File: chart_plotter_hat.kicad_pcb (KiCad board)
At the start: 4 copper layers, 65 x 56 mm, 52 parts, among them J1 Conn_02x03_Odd_Even, J2 Conn_01x04, J3 40HAT, J4 Conn_01x04, J5 Conn_01x04, J6 Conn_01x02, J7 Conn_01x04, J8 Conn_02x03_Odd_Even, J9 Conn_01x04, Q1 DMG2305UX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

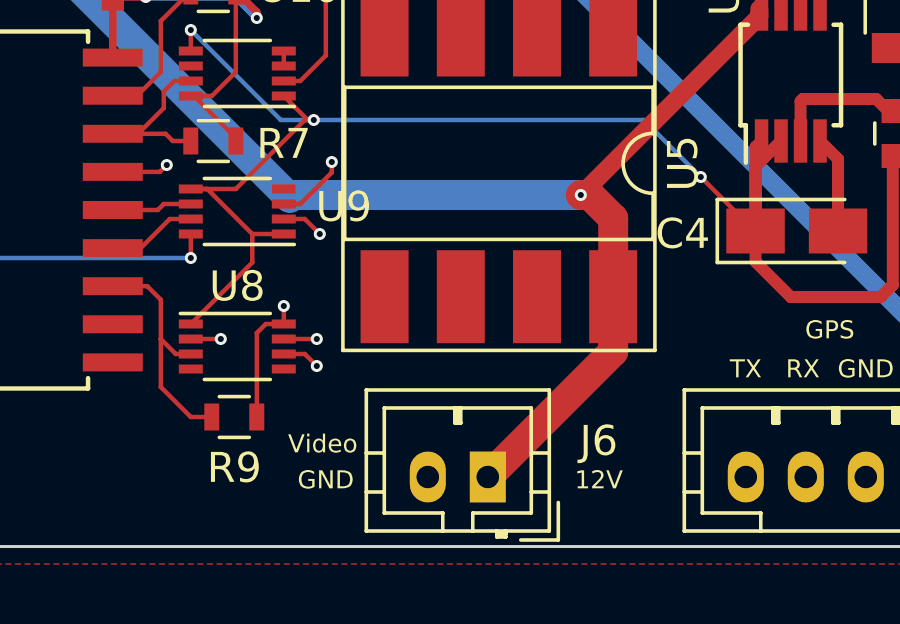
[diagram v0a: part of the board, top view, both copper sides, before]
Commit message: Fixed relay wiring
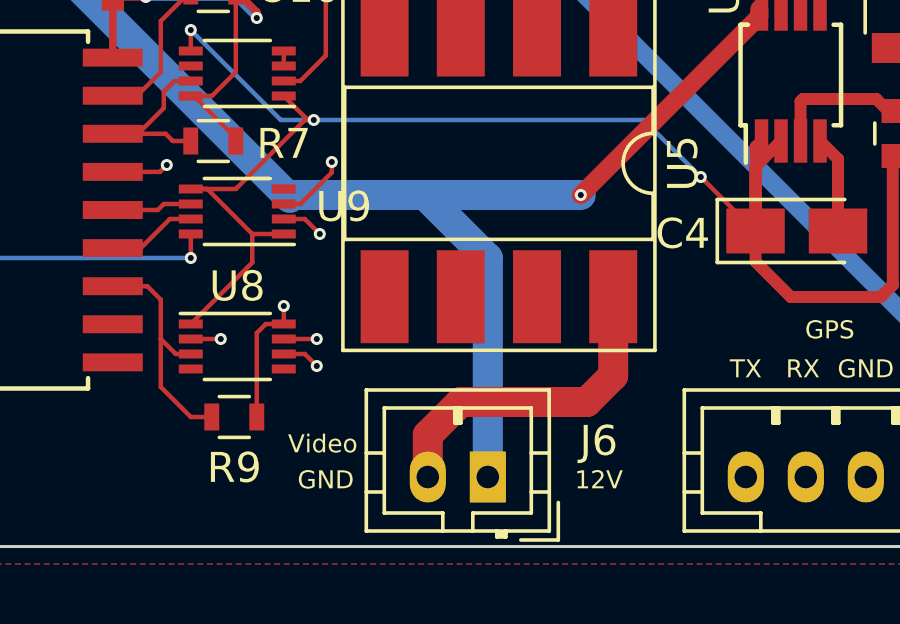
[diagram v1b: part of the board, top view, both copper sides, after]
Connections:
- J6 pad 2: GND -> Net-(J6-Pad2)
- U5 pad 8: +12V -> Net-(J6-Pad2)
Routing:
- net Net-(J6-Pad2): track 0.00 -> 11.0 mm
- net +12V: track 92.2 -> 90.7 mm

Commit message: Updated from rev B
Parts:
- added C12: .1uF, Capacitors_SMD:C_0603, F.Cu at (100.3, 96.0)
- added C13: .1uF, Capacitors_SMD:C_0603, F.Cu at (166.4, 97.2)
- added C14: .1uF, Capacitors_SMD:C_0603, F.Cu at (173.0, 90.8)
- added C15: .1uF, Capacitors_SMD:C_0603, F.Cu at (88.7, 101.3)
- added C16: 18pF, Capacitors_SMD:C_0603, F.Cu at (176.8, 88.4)
- added C17: 18pF, Capacitors_SMD:C_0603, F.Cu at (173.0, 93.1)
- added D3: PMEG3020EH, Diodes_SMD:D_SOD-123, F.Cu at (82.6, 95.5)
- added JP1: SolderJumper_2_Open, CustomComponents:SolderJumper-2_P1.3mm_Open_RoundedPad1.0x1.5mm, F.Cu at (134.1, 88.5)
- added L1: 10uH, Capacitors_SMD:C_0603, F.Cu at (130.7, 90.4)
- added R11: 10K, Resistors_SMD:R_0603, F.Cu at (176.7, 90.8)
- added R12: 10K, Resistors_SMD:R_0603, F.Cu at (180.5, 87.7)
- added R13: 10K, Resistors_SMD:R_0603, F.Cu at (174.0, 95.5)
- C10, C11: value 18pF -> .1uF
- J1: value Conn_02x03_Odd_Even -> JST PH; footprint CustomComponents:BOX-HEADER6 -> Connectors_JST:JST_PH_B6B-PH-K_06x2.00mm_Straight
- J2, J4, J5, J7: value Conn_01x04 -> JST PH
- J6: value Conn_01x02 -> JST PH
- J9: value Conn_01x04 -> JST PH; footprint Connectors_JST:JST_PH_B4B-PH-K_04x2.00mm_Straight -> Connectors_JST:JST_PH_B3B-PH-K_03x2.00mm_Straight
- R2, R4: value 680 -> 1.6K
- R3: value 330 -> 750
- R7: value 10K -> 39K
- R9: value 10K -> 12K
- U6: value MCP2551-I-SN -> MCP2515-xSO; footprint Housings_SOIC:SOIC-8_3.9x4.9mm_Pitch1.27mm -> Housings_SOIC:SOIC-18W_7.5x11.6mm_Pitch1.27mm
- U7: value MCP2515-xSO -> MCP2551-I-SN; footprint Housings_SOIC:SOIC-18W_7.5x11.6mm_Pitch1.27mm -> Housings_SOIC:SOIC-8_3.9x4.9mm_Pitch1.27mm
- Y1: value 16MHz -> 16 MHz
- moved C11 90.5 mm to (177.4, 85.3)
- moved C10 88.3 mm to (173.0, 88.4)
- moved Y1 85.9 mm to (166.6, 83.9)
- moved C9 76.2 mm to (164.4, 94.8), turned to 0 degrees
- moved U9 74.8 mm to (178.2, 82.3), turned to 0 degrees
- moved R5 74.6 mm to (180.5, 90.2)
- moved C8 67.3 mm to (170.3, 97.2), turned to 0 degrees
- moved U8 52.8 mm to (157.9, 95.7)
- moved U10 45.5 mm to (152.3, 95.7), turned to 0 degrees
- moved J9 38.7 mm to (117.6, 114.2), turned to 180 degrees
- moved R9 27.8 mm to (131.2, 98.8)
- moved R7 26.0 mm to (131.2, 95.6), turned to 180 degrees
- moved R3 21.4 mm to (74.7, 96.8)
- moved D2 20.9 mm to (74.3, 94.1)
- moved D1 20.7 mm to (74.3, 89.7)
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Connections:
- net SS renamed CS
- C10 pad 1: Net-(C10-Pad1) -> GND
- C10 pad 2: GND -> +3V3
- C11 pad 1: Net-(C11-Pad1) -> GND
- C11 pad 2: GND -> +5V
- C5 pad 1: +3V3 -> Net-(C5-Pad1)
- C8 pad 1: +5V -> GND
- C8 pad 2: GND -> +3V3
- C9 pad 1: +5V -> GND
- C9 pad 2: GND -> +5V
- D2 pad 2: SHUTDOWN -> Net-(D2-Pad2)
- J2 pad 1: +12V -> /12VBAT
- J3 pad 11: CAN_INT -> (no net)
- J3 pad 12: XCLR -> CAN_CS
- J3 pad 13: (no net) -> BUTTON
- J3 pad 18: (no net) -> XCLR
- J3 pad 26: CSS -> (no net)
- J3 pad 35: (no net) -> MISO-2
- J3 pad 36: (no net) -> CAN_RST
- J3 pad 38: (no net) -> MOSI-2
- J3 pad 40: (no net) -> SCK-2
- J6 pad 1: +12V -> Net-(J6-Pad1)
- J6 pad 2: Net-(J6-Pad2) -> GND
- J9 pad 1: +12V -> /12VBAT
- J9 pad 2: Net-(J9-Pad2) -> +5V
- J9 pad 3: Net-(J9-Pad3) -> GND
- R2 pad 2: +5V -> GND
- R5 pad 1: Net-(R5-Pad1) -> CAN_INT
- R5 pad 2: +5V -> +3V3
- R7 pad 1: CAN-SS -> /12VBAT
- R7 pad 2: +5V -> Net-(JP1-Pad2)
- R9 pad 1: INT -> GND
- R9 pad 2: +5V -> Net-(JP1-Pad2)
- U1 pad 1: MCU_RUNNING -> (no net)
- U1 pad 12: (no net) -> Net-(D2-Pad2)
- U1 pad 13: (no net) -> MCU_RUNNING
- U1 pad 18: +3V3 -> Net-(C5-Pad1)
- U10 pad 2: CSS -> CAN_CS
- U10 pad 3: GND -> CAN_RST
- U10 pad 6: GND -> CRST
- U10 pad 7: CAN-SS -> CCS
- U5 pad 2: Net-(R2-Pad1) -> +5V
- U5 pad 3: GND -> Net-(R2-Pad1)
- U5 pad 5: GND -> Net-(J6-Pad1)
- U5 pad 8: Net-(J6-Pad2) -> +12V
- U6 pad 2: GND -> Net-(U6-Pad2)
- U6 pad 3: +5V -> (no net)
- U6 pad 4: Net-(U6-Pad4) -> (no net)
- U6 pad 6: Net-(J9-Pad2) -> (no net)
- U6 pad 7: Net-(J9-Pad3) -> Net-(C16-Pad1)
- U6 pad 8: GND -> Net-(C17-Pad1)
- U7 pad 2: Net-(U6-Pad4) -> GND
- U7 pad 3: (no net) -> +5V
- U7 pad 4: (no net) -> Net-(U6-Pad2)
- U7 pad 7: Net-(C10-Pad1) -> (no net)
- U7 pad 8: Net-(C11-Pad1) -> GND
- U8 pad 2: CAN-MISO -> CAN_INT
- U8 pad 3: INT -> MISO-2
- U8 pad 6: CAN_INT -> CAN_SO
- U8 pad 7: MISO -> INT
- U9 pad 2: SCK -> MOSI-2
- U9 pad 3: MOSI -> SCK-2
- U9 pad 6: CAN-MOSI -> CAN_SCK
- U9 pad 7: CAN-SCK -> CAN_SI
- Y1 pad 1: Net-(C10-Pad1) -> Net-(C16-Pad1)
- Y1 pad 2: Net-(C11-Pad1) -> Net-(C17-Pad1)
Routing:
- net +5V: track 134.3 -> 8.59 mm, vias 8 -> 0
- net +12V: track 90.7 -> 16.6 mm, vias 1 -> 0
- net SerialRX: track 66.1 -> 0.00 mm
- net SerialTX: track 65.4 -> 0.00 mm, vias 1 -> 0
- net CAN_INT: track 63.1 -> 0.00 mm, vias 2 -> 0
- net +3V3: track 172.3 -> 116.4 mm, vias 9 -> 4
- net CSS: track 42.9 -> 0.00 mm, vias 2 -> 0
- net SHUTDOWN: track 59.3 -> 34.8 mm, vias 4 -> 1
- net SCK: track 77.0 -> 53.7 mm, vias 3 -> 1
- net MISO: track 78.6 -> 56.7 mm, vias 3 -> 2
- net BUTTON: track 43.0 -> 63.0 mm, vias 1 -> 2
- net MOSI: track 76.3 -> 57.4 mm, vias 2 -> 1
- net Net-(C10-Pad1): track 16.5 -> 0.00 mm
- net MCU_RUNNING: track 32.7 -> 47.7 mm, vias 1 -> 2
- net Net-(JP1-Pad2): track 0.00 -> 11.8 mm
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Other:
- board text added: "Barometer"
- board text added: "Rev C"
- board text added: "Sense"
- board text added: "Voltmeter"
- board text removed: "Hi"
- board text removed: "Lo"
- board text removed: "Pressure"
- board text removed: "Rev B"

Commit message: First pass at layout
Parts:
- removed C13, C14, C8, C9: .1uF, Capacitors_SMD:C_0603
- removed U10, U9: 74LVC2T45DC, Housings_SSOP:VSSOP-8_2.3x2mm_Pitch0.5mm
- added H5: LightPipeMount, project_footprints:SMFLPX.X-light-pipe-adapter-smd, F.Cu at (82.9, 103.8)
- added H6: LightPipeMount, project_footprints:SMFLPX.X-light-pipe-adapter-smd, F.Cu at (131.2, 106.7)
- added J10: JST PH, Connectors_JST:JST_PH_B2B-PH-K_02x2.00mm_Straight, F.Cu at (90.9, 114.1)
- added Q3: DMG2305UX, TO_SOT_Packages_SMD:SOT-23, F.Cu at (107.5, 88.2)
- added R14: 47K, Resistors_SMD:R_0603, F.Cu at (107.3, 84.5)
- U8: value 74LVC2T45DC -> ST2378E; footprint Housings_SSOP:VSSOP-8_2.3x2mm_Pitch0.5mm -> Housings_SSOP:TSSOP-20_4.4x6.5mm_Pitch0.65mm
- Y1: footprint Crystals:Crystal_HC49-U_Vertical -> Crystals:Crystal_SMD_SeikoEpson_TSX3225-4pin_3.2x2.5mm
- moved C16 82.9 mm to (97.8, 113.5)
- moved C17 74.2 mm to (101.7, 113.5), turned to 180 degrees
- moved Y1 72.0 mm to (99.7, 110.6)
- moved R3 66.8 mm to (140.4, 108.8)
- moved R5 62.2 mm to (120.0, 75.8), turned to 180 degrees
- moved R12 61.3 mm to (120.0, 77.8), turned to 180 degrees
- moved D2 58.3 mm to (131.2, 106.7), turned to 90 degrees
- moved C10 48.1 mm to (128.4, 70.2), turned to 180 degrees
- moved C11 47.1 mm to (132.8, 70.2)
- moved R13 44.4 mm to (136.1, 72.4), turned to 270 degrees
- moved R11 43.0 mm to (136.1, 76.5), turned to 270 degrees
- moved U8 34.0 mm to (130.6, 75.4)
- moved D1 16.5 mm to (82.9, 103.8)
- moved R4 9.74 mm to (82.8, 96.8)
- moved C12 8.76 mm to (91.5, 96.4), turned to 0 degrees
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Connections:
- C10 pad 2: +3V3 -> VEE
- C6 pad 1: +3V3 -> VEE
- J1 pad 1: +3V3 -> VEE
- J3 pad 37: (no net) -> CAN_INT
- R12 pad 2: +3V3 -> VEE
- R29 pad 1: +3V3 -> VEE
- R5 pad 2: +3V3 -> VEE
- R6 pad 1: +3V3 -> VEE
- R8 pad 1: +3V3 -> VEE
- U1 pad 11: (no net) -> VEE_ENABLE
- U2 pad 8: +3V3 -> VEE
- U7 pad 6: (no net) -> CAN_LO
- U7 pad 7: (no net) -> CAN_HI
- U8 pad 1: +3V3 -> VEE
- U8 pad 3: MISO-2 -> CAN_SO
- U8 pad 4: GND -> MOSI-2
- U8 pad 5: GND -> CAN_SCK
- U8 pad 6: CAN_SO -> CAN_CS
- U8 pad 7: INT -> CRST
- U8 pad 8: +5V -> (no net)
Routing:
- net +5V: track 8.59 -> 167.6 mm, vias 0 -> 5
- net /12VBAT: track 9.63 -> 92.6 mm
- net VEE: track 0.00 -> 81.3 mm, vias 0 -> 6
- net SerialRX: track 0.00 -> 73.4 mm
- net SerialTX: track 0.00 -> 70.8 mm, vias 0 -> 1
- net CCS: track 0.00 -> 53.9 mm, vias 0 -> 2
- net INT: track 0.00 -> 52.9 mm, vias 0 -> 3
- net CAN_SI: track 0.00 -> 50.9 mm, vias 0 -> 2
- net +12V: track 16.6 -> 61.8 mm, vias 0 -> 2
- net CRST: track 0.00 -> 41.5 mm, vias 0 -> 2
- net CAN_SO: track 0.00 -> 40.4 mm, vias 0 -> 2
- net CAN_CS: track 0.00 -> 38.8 mm, vias 0 -> 2
- net CAN_SCK: track 0.00 -> 38.1 mm, vias 0 -> 2
- net A7: track 15.7 -> 52.6 mm
- net A6: track 12.3 -> 45.5 mm, vias 1 -> 2
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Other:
- board text added: "CAN"
- board text added: "HI"
- board text added: "LO"

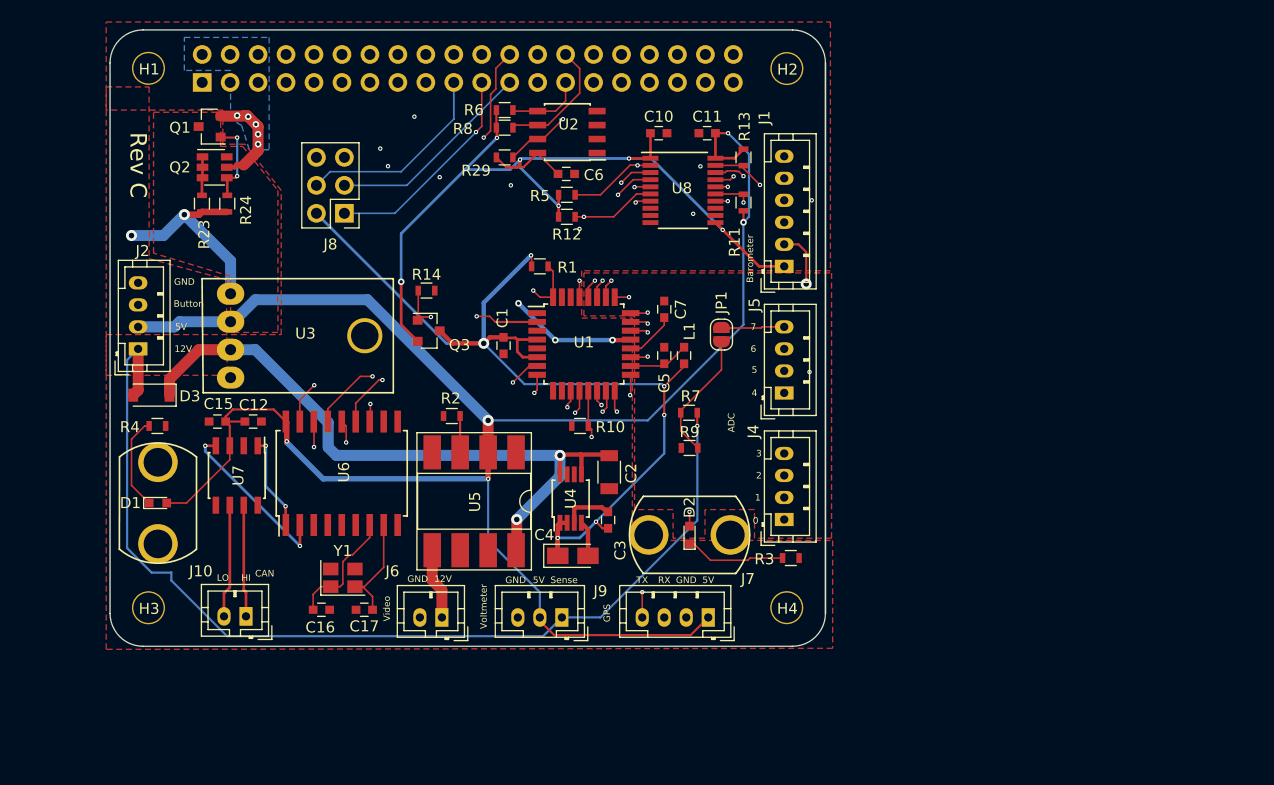
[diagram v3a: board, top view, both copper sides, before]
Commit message: Fixed 3.3aux switch and mounting hole sizes
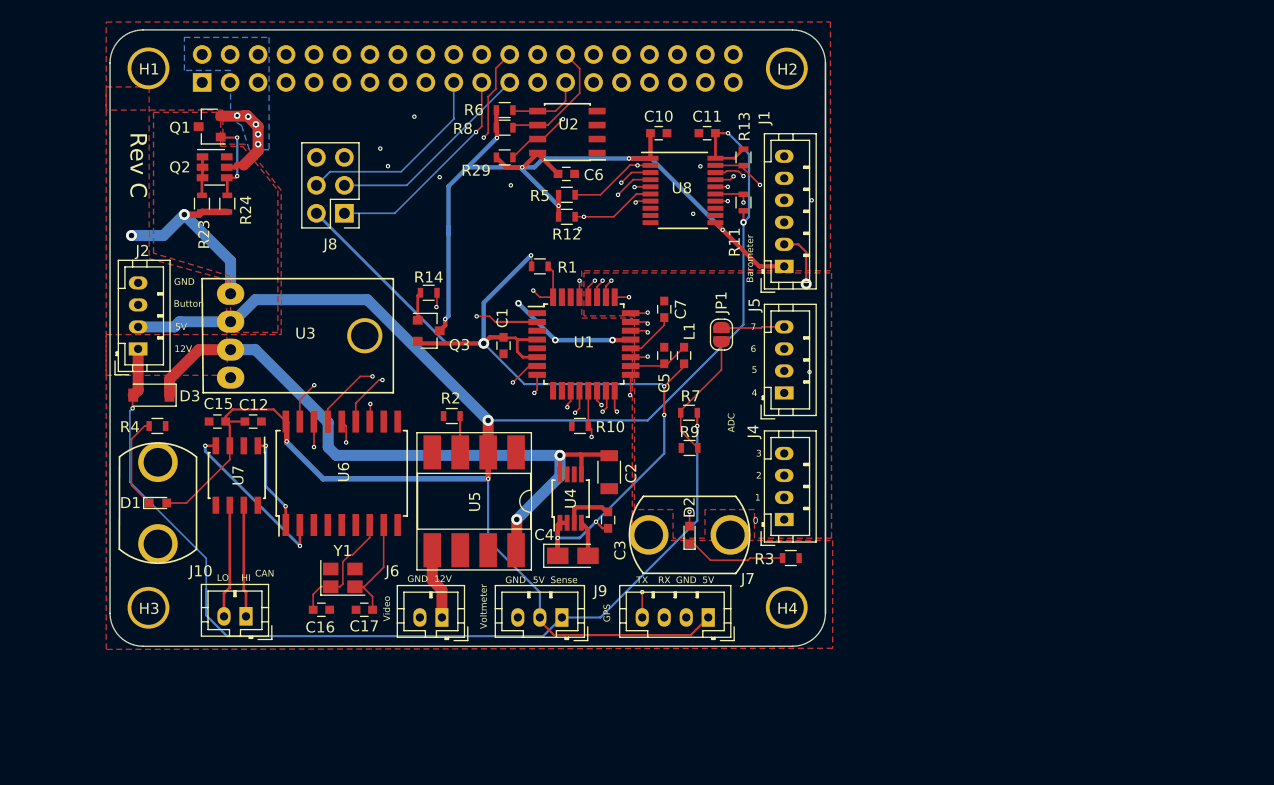
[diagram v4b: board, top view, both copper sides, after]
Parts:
- R14: value 47K -> 220
- moved R14 0.28 mm to (107.5, 84.7), turned to 180 degrees
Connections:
- Q3 pad 1: VEE_ENABLE -> Net-(Q3-Pad1)
- Q3 pad 2: VEE -> +3V3
- Q3 pad 3: +3V3 -> VEE
- R14 pad 2: GND -> Net-(Q3-Pad1)
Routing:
- net /12VBAT: track 92.6 -> 86.9 mm, vias 1 -> 2
- net VEE: track 81.3 -> 76.8 mm
- net Net-(Q3-Pad1): track 0.00 -> 3.03 mm
- net VEE_ENABLE: track 21.5 -> 19.3 mm
- net +3V3: track 90.2 -> 91.8 mm

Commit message: Added CAN_RST pull-ups
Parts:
- added R15: 10K, Resistors_SMD:R_0603, F.Cu at (133.2, 80.2)
- added R16: 10K, Resistors_SMD:R_0603, F.Cu at (127.8, 80.1)
- R3: value 750 -> 120
- R4: value 1.6K -> 300
- U3: value MPM3610-adafruit -> MPM3610-5.0-adafruit
- U4: value LT1762 -> LT1762-3.3
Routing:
- net +5V: track 167.6 -> 175.4 mm, vias 5 -> 6
- net CAN_RST: track 17.4 -> 22.3 mm
- net CRST: track 41.5 -> 45.4 mm
- net VEE: track 76.8 -> 78.2 mm

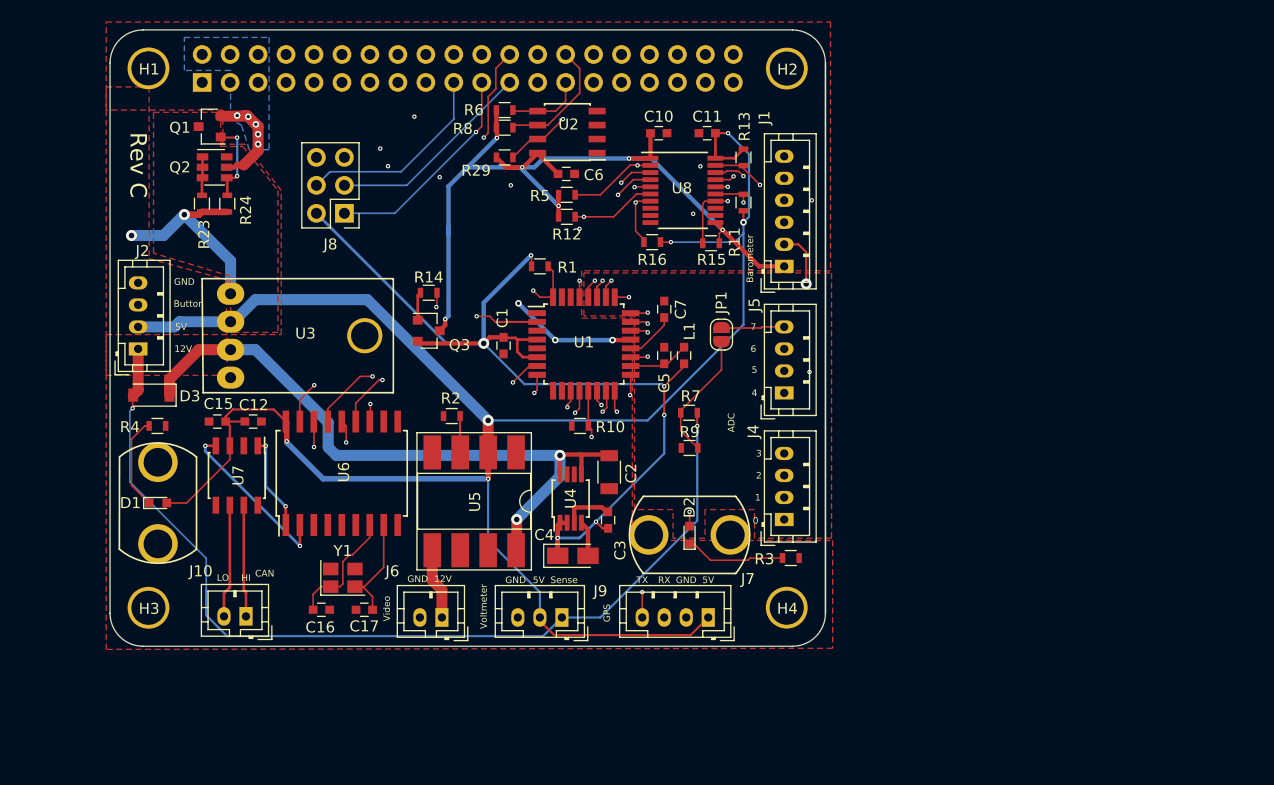
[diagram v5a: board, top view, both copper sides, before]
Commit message: Crystal was miswired
Replaced schematic symbol for Y1
Rewired Y1 in pcb
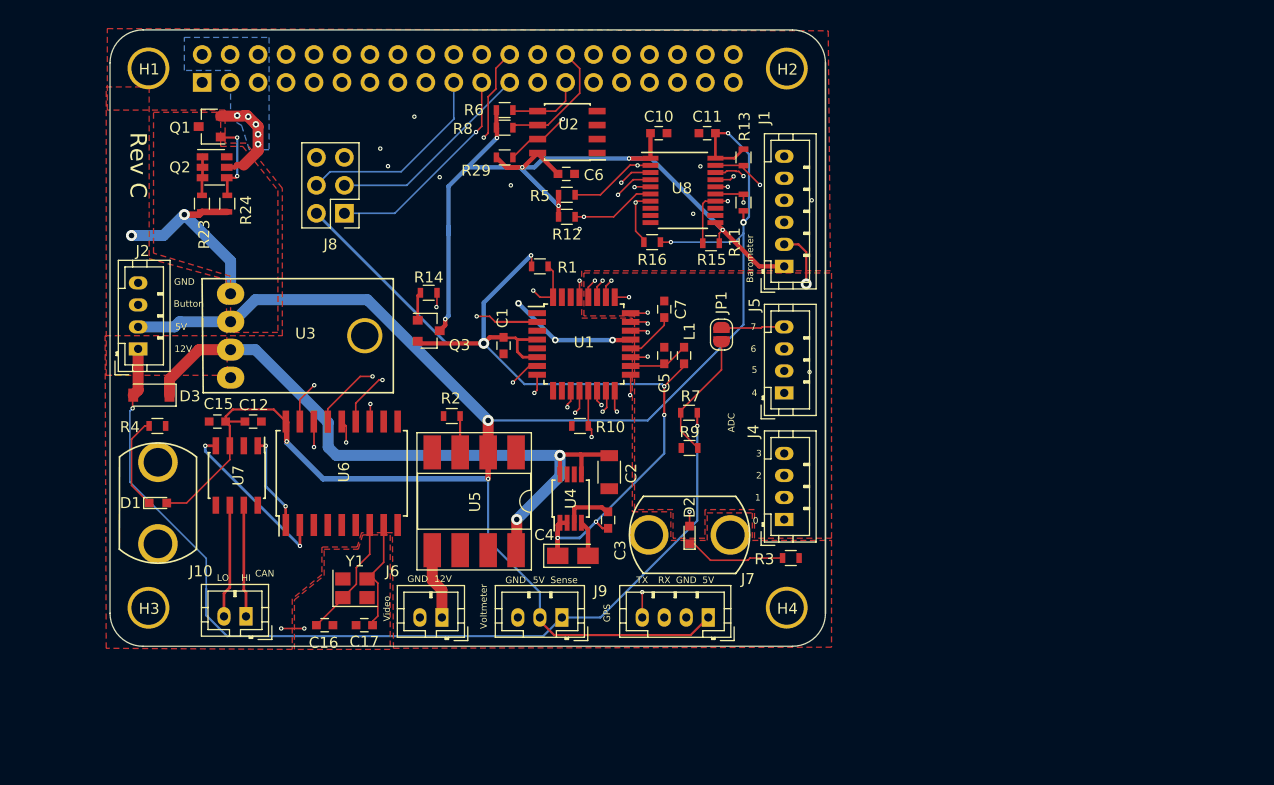
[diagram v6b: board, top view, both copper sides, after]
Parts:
- Y1: value 16 MHz -> 16MHz; footprint Crystals:Crystal_SMD_SeikoEpson_TSX3225-4pin_3.2x2.5mm -> Crystals:Crystal_SMD_TXC_7M-4pin_3.2x2.5mm
- moved Y1 1.45 mm to (100.8, 111.5)
- moved C16 1.43 mm to (98.0, 114.9)
- moved C17 1.40 mm to (101.7, 114.9)
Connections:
- Y1 pad 2: Net-(C17-Pad1) -> GND
- Y1 pad 3: (no net) -> Net-(C17-Pad1)
- Y1 pad 4: (no net) -> GND
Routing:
- net GND: track 38.6 -> 40.7 mm, vias 6 -> 8
